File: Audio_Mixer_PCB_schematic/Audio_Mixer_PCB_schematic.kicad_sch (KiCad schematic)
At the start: 75 parts, among them J1 AudioJack3, J2 AudioJack3, J3 AudioJack3, U1 TL074, U2 TL074, U3 TL074, U4 TL074, U5 TL074

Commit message: part assembly1
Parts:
- added D1: LED, LED_THT:LED_D5.0mm, symbol Device:LED
- added R36: 3.3k, Resistor_SMD:R_0805_2012Metric_Pad1.20x1.40mm_HandSolder, symbol Device:R
- added SW1: SW_SPST, LED_THT:LED_D5.0mm, symbol Switch:SW_SPST
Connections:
- net +9V: now also R36.2, SW1.2 (B); no longer BT1.1 (+)
- net GND: now also D1.1 (K)
- new net: D1.2 (A), R36.1
- new net: BT1.1 (+), SW1.1 (A)
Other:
- moved on the sheet: BT1

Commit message: updated parts
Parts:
- RV1, RV2, RV3, RV4, RV5, RV6: footprint (none) -> Potentiometer_THT:Tayda_60mm_Slider
- SW1: footprint LED_THT:LED_D5.0mm -> (none)
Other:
- moved on the sheet: U5E
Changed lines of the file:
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@@
 	(wire
 		(pts
-			(xy 198.12 125.73) (xy 205.74 125.73)
+			(xy 196.85 125.73) (xy 205.74 125.73)
 		)
 		(stroke
@@
 	(wire
 		(pts
-			(xy 198.12 140.97) (xy 205.74 140.97)
+			(xy 196.85 140.97) (xy 205.74 140.97)
 		)
 		(stroke
@@
 			)
 		)
-		(property "Footprint" ""
+		(property "Footprint" "Potentiometer_THT:Tayda_60mm_Slider"
 			(at 285.75 189.23 0)
 			(effects
@@
 			)
 		)
-		(property "Footprint" ""
+		(property "Footprint" "Potentiometer_THT:Tayda_60mm_Slider"
 			(at 220.98 57.15 0)
 			(effects
@@
 			)
 		)
-		(property "Footprint" ""
+		(property "Footprint" "Potentiometer_THT:Tayda_60mm_Slider"
 			(at 224.79 76.2 0)
 			(effects
@@
 	(symbol
 		(lib_id "Amplifier_Operational:TL074")
-		(at 200.66 133.35 0)
+		(at 199.39 133.35 0)
 		(mirror x)
 		(unit 5)
@@
 		(dnp no)
 		(property "Reference" "U5"
-			(at 198.628 124.206 0)
+			(at 197.358 124.206 0)
 			(effects
 				(font
@@
 		)
 		(property "Value" "TL074"
-			(at 198.628 121.666 0)
+			(at 197.358 121.666 0)
 			(effects
 				(font
@@
 		)
 		(property "Footprint" "Package_SO:SOIC-14_3.9x8.7mm_P1.27mm"
-			(at 199.39 135.89 0)
+			(at 198.12 135.89 0)
 			(effects
 				(font
@@
 		)
 		(property "Datasheet" "http://www.ti.com/lit/ds/symlink/tl071.pdf"
-			(at 201.93 138.43 0)
+			(at 200.66 138.43 0)
 			(effects
 				(font
@@
 		)
 		(property "Description" "Quad Low-Noise JFET-Input Operational Amplifiers, DIP-14/SOIC-14"
-			(at 200.66 133.35 0)
+			(at 199.39 133.35 0)
 			(effects
 				(font
@@
 			)
 		)
-		(property "Footprint" ""
+		(property "Footprint" "Potentiometer_THT:Tayda_60mm_Slider"
 			(at 285.75 229.87 0)
 			(effects
@@
 			)
 		)
-		(property "Footprint" "LED_THT:LED_D5.0mm"
+		(property "Footprint" ""
 			(at 237.49 127 0)
 			(effects
@@
 			)
 		)
-		(property "Footprint" ""
+		(property "Footprint" "Potentiometer_THT:Tayda_60mm_Slider"
 			(at 285.75 208.28 0)
 			(effects
@@
 			)
 		)
-		(property "Footprint" ""
+		(property "Footprint" "Potentiometer_THT:Tayda_60mm_Slider"
 			(at 224.79 97.79 0)
 			(effects

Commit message: Finished schematic wiring and mapped hardware footprints
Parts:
- removed J1, J2, J3: AudioJack3, symbol Connector_Audio:AudioJack3
- added J7, J8, J9: AudioJack3_SwitchTR, Connector_Audio:Jack_3.5mm_CUI_SJ1-3525N_Horizontal, symbol Connector_Audio:AudioJack3_SwitchTR
- RV1, RV2, RV3, RV4, RV5, RV6: footprint Potentiometer_THT:Tayda_60mm_Slider -> Connector_PinHeader_2.54mm:PinHeader_1x03_P2.54mm_Vertical
- SW1: footprint (none) -> Connector_PinHeader_2.54mm:PinHeader_1x02_P2.54mm_Vertical
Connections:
- net GND: now also J7.S, J8.S, J9.S
- net at C4.2, R35.1: now also J9.R, J9.T
- net at R21.1: now also J8.R
- net at R10.1: now also J7.R
- net at R11.1: now also J7.T
- net at R20.1: now also J8.T
- no-connect marks 0 -> 6

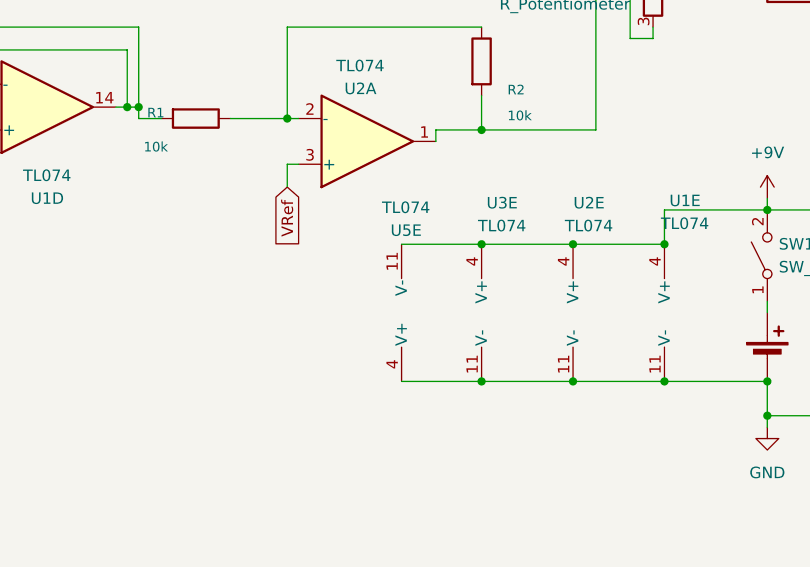
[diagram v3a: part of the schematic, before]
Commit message: fixed minor battery schematic bugs. started route tracing components in pcb.
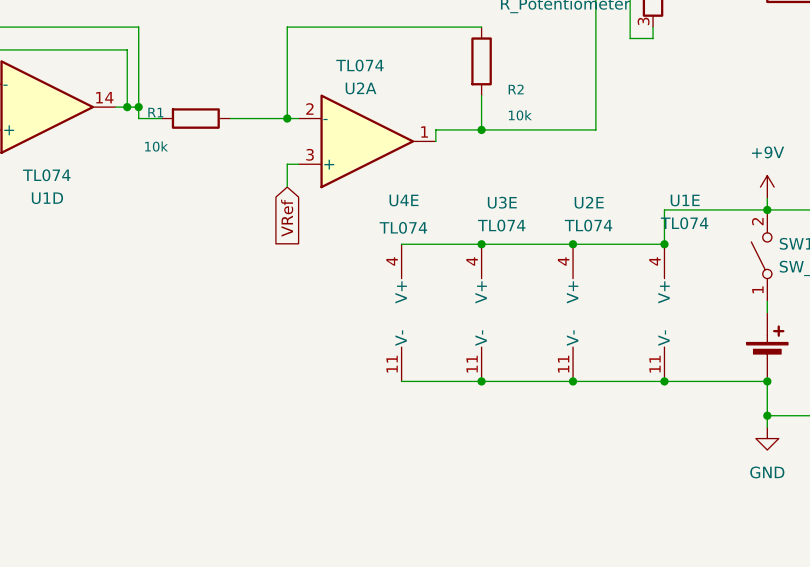
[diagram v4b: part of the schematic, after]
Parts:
- renumbered U5 to U4
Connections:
- net +9V: now also U4.4 (V+); no longer U4.11 (V-)
- net GND: now also U4.11 (V-); no longer U4.4 (V+)
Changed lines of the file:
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@@
 		(lib_id "Amplifier_Operational:TL074")
 		(at 199.39 133.35 0)
-		(mirror x)
 		(unit 5)
 		(body_style 1)
@@
 		(in_pos_files yes)
 		(dnp no)
-		(property "Reference" "U5"
-			(at 197.358 124.206 0)
+		(property "Reference" "U4"
+			(at 197.104 120.904 0)
 			(show_name no)
 			(do_not_autoplace no)
@@
 		)
 		(property "Value" "TL074"
-			(at 197.358 121.666 0)
+			(at 197.104 123.952 0)
 			(show_name no)
 			(do_not_autoplace no)
@@
 		)
 		(property "Footprint" "Package_SO:SOIC-14_3.9x8.7mm_P1.27mm"
-			(at 198.12 135.89 0)
+			(at 198.12 130.81 0)
 			(hide yes)
 			(show_name no)
@@
 		)
 		(property "Datasheet" "http://www.ti.com/lit/ds/symlink/tl071.pdf"
-			(at 200.66 138.43 0)
+			(at 200.66 128.27 0)
 			(hide yes)
 			(show_name no)
@@
 			(project "Audio_Mixer_PCB_schematic"
 				(path "/d53613de-2b1a-4eeb-bd13-9c09b173f45c"
-					(reference "U5")
+					(reference "U4")
 					(unit 5)
 				)

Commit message: routed all traces, moved components to better looking areas, fixed all DRC errors
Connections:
- net 0 is gone; now on net GND: C15.2, C21.2, C23.2, C9.2
- net at R8.1, U2.7: now also R23.1; no longer R23.2
- net at R24.1, R25.2, U4.2 (-): now also R23.2; no longer R23.1
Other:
- moved on the sheet: R23
